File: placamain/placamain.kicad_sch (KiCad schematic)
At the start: 38 parts, among them J1 Conn_01x10_Pin, J2 Conn_01x10_Pin, Q1 PN3643, U10 LF356, U2 LF356, U3 LF356, U4 LF356, U5 AD548JN, U6 LF356, U7 LF356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

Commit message: empieza parte de los comparadores LM393
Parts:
- added C5: valor?, symbol Device:C_Small
- added D2: ?, symbol Device:D_Zener
- added Q2: BC559, symbol Simulation_SPICE:PNP
- added R7: 7,5K, symbol Device:R
- D1: value D_Zener -> ?
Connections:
- net -15V: now also C5.2, Q2.3 (E), R7.1
- net at J1.10 (Pin_10), R9.1: now also Q2.1 (C)
- net at D1.1 (K), J1.6 (Pin_6), U2.3 (+): now also D2.1 (K)
- new net: C5.1, D2.2 (A), Q2.2 (B), R7.2
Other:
- moved on the sheet: U9A, U9B, U9C

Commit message: Resistencias lado comparador
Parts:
- added R1: 3,9k, symbol Device:R
- added R2: 4,8k, symbol Device:R
- added R3: 3,6k, symbol Device:R
- added w4: 0, symbol Device:R
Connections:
- net GND: now also R2.2
- net at U9.6 (-): now also R2.1, R3.1
- net at U9.7: now also R1.2
- net at J1.4 (Pin_4): now also w4.2
- net at U9.4 (V-): now also R3.2
- new net: R1.1, w4.1
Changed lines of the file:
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@@
   (junction (at 53.34 185.42) (diameter 0) (color 0 0 0 0)
   )
+  (junction (at 38.1 24.13) (diameter 0) (color 0 0 0 0)
+  )
   (junction (at 50.8 147.32) (diameter 0) (color 0 0 0 0)
   )
@@
     (stroke (width 0) (type default))
   )
+  (wire (pts (xy 52.07 21.59) (xy 52.07 29.21))
+    (stroke (width 0) (type default))
+  )
   (wire (pts (xy 57.15 137.16) (xy 48.26 137.16))
     (stroke (width 0) (type default))
@@
     (stroke (width 0) (type default))
   )
+  (wire (pts (xy 20.32 142.24) (xy 45.72 142.24))
+    (stroke (width 0) (type default))
+  )
   (wire (pts (xy 119.38 107.95) (xy 119.38 115.57))
     (stroke (width 0) (type default))
@@
     (stroke (width 0) (type default))
   )
+  (wire (pts (xy 45.72 21.59) (xy 52.07 21.59))
+    (stroke (width 0) (type default))
+  )
+  (wire (pts (xy 54.61 26.67) (xy 54.61 58.42))
+    (stroke (width 0) (type default))
+  )
   (wire (pts (xy 69.85 106.68) (xy 77.47 106.68))
     (stroke (width 0) (type default))
@@
     (stroke (width 0) (type default))
   )
+  (wire (pts (xy 38.1 21.59) (xy 38.1 24.13))
+    (stroke (width 0) (type default))
+  )
   (wire (pts (xy 67.31 180.34) (xy 71.12 180.34))
     (stroke (width 0) (type default))
@@
     (stroke (width 0) (type default))
   )
+  (wire (pts (xy 45.72 142.24) (xy 45.72 147.32))
+    (stroke (width 0) (type default))
+  )
+  (wire (pts (xy 27.94 54.61) (xy 33.02 54.61))
+    (stroke (width 0) (type default))
+  )
   (wire (pts (xy 69.85 163.83) (xy 69.85 168.91))
     (stroke (width 0) (type default))
@@
     (stroke (width 0) (type default))
   )
+  (wire (pts (xy 40.64 58.42) (xy 54.61 58.42))
+    (stroke (width 0) (type default))
+  )
   (wire (pts (xy 77.47 173.99) (xy 77.47 185.42))
     (stroke (width 0) (type default))
   )
+  (wire (pts (xy 20.32 54.61) (xy 20.32 142.24))
+    (stroke (width 0) (type default))
+  )
   (wire (pts (xy 38.1 165.1) (xy 50.8 165.1))
     (stroke (width 0) (type default))
@@
     (stroke (width 0) (type default))
   )
+  (wire (pts (xy 55.88 52.07) (xy 48.26 52.07))
+    (stroke (width 0) (type default))
+  )
   (wire (pts (xy 26.67 161.29) (xy 55.88 161.29))
     (stroke (width 0) (type default))
@@
     (stroke (width 0) (type default))
   )
+  (wire (pts (xy 38.1 24.13) (xy 27.94 24.13))
+    (stroke (width 0) (type default))
+  )
   (wire (pts (xy 106.68 147.32) (xy 106.68 146.05))
     (stroke (width 0) (type default))
@@
     (stroke (width 0) (type default))
   )
+  (wire (pts (xy 45.72 26.67) (xy 54.61 26.67))
+    (stroke (width 0) (type default))
+  )
   (wire (pts (xy 53.34 180.34) (xy 53.34 185.42))
     (stroke (width 0) (type default))
@@
     (stroke (width 0) (type default))
   )
+  (wire (pts (xy 20.32 46.99) (xy 20.32 16.51))
+    (stroke (width 0) (type default))
+  )
   (wire (pts (xy 53.34 88.9) (xy 57.15 88.9))
     (stroke (width 0) (type default))
@@
     (stroke (width 0) (type default))
   )
+  (wire (pts (xy 20.32 16.51) (xy 38.1 16.51))
+    (stroke (width 0) (type default))
+  )
   (wire (pts (xy 121.92 143.51) (xy 121.92 147.32))
     (stroke (width 0) (type default))
@@
     (stroke (width 0) (type default))
   )
+  (wire (pts (xy 55.88 16.51) (xy 55.88 52.07))
+    (stroke (width 0) (type default))
+  )
+  (wire (pts (xy 45.72 16.51) (xy 55.88 16.51))
+    (stroke (width 0) (type default))
+  )
   (wire (pts (xy 86.36 123.19) (xy 86.36 114.3))
     (stroke (width 0) (type default))
@@
   )
   (wire (pts (xy 146.05 110.49) (xy 147.32 110.49))
+    (stroke (width 0) (type default))
+  )
+  (wire (pts (xy 38.1 24.13) (xy 38.1 26.67))
+    (stroke (width 0) (type default))
+  )
+  (wire (pts (xy 27.94 24.13) (xy 27.94 54.61))
     (stroke (width 0) (type default))
   )
@@
     )
   )
+  (symbol (lib_id "Device:R") (at 20.32 50.8 0) (unit 1)
+    (in_bom yes) (on_board yes) (dnp no) (fields_autoplaced)
+    (property "Reference" "w4" (at 22.86 50.165 0)
+      (effects (font (size 1.27 1.27)) (justify left))
+    )
+    (property "Value" "0" (at 22.86 52.705 0)
+      (effects (font (size 1.27 1.27)) (justify left))
+    )
+    (property "Footprint" "" (at 18.542 50.8 90)
+      (effects (font (size 1.27 1.27)) hide)
+    )
+    (property "Datasheet" "~" (at 20.32 50.8 0)
+      (effects (font (size 1.27 1.27)) hide)
+    )
+    (pin "1")
+    (pin "2")
+    (instances
+      (project "placamain"
+        (path "/97204b45-cd64-488c-9a18-9c4a16d0810d"
+          (reference "w4") (unit 1)
+        )
+      )
+    )
+  )
   (symbol (lib_id "Amplifier_Operational:LF356") (at 170.18 101.6 0) (unit 1)
     (in_bom yes) (on_board yes) (dnp no)
@@
     )
   )
+  (symbol (lib_id "Device:R") (at 41.91 16.51 90) (unit 1)
+    (in_bom yes) (on_board yes) (dnp no)
+    (property "Reference" "R1" (at 44.45 13.97 90)
+      (effects (font (size 1.27 1.27)) (justify right))
+    )
+    (property "Value" "3,9k" (at 39.37 13.97 90)
+      (effects (font (size 1.27 1.27)) (justify right))
+    )
+    (property "Footprint" "" (at 41.91 18.288 90)
+      (effects (font (size 1.27 1.27)) hide)
+    )
+    (property "Datasheet" "~" (at 41.91 16.51 0)
+      (effects (font (size 1.27 1.27)) hide)
+    )
+    (pin "1")
+    (pin "2")
+    (instances
+      (project "placamain"
+        (path "/97204b45-cd64-488c-9a18-9c4a16d0810d"
+          (reference "R1") (unit 1)
+        )
+      )
+    )
+  )
+  (symbol (lib_id "Device:R") (at 41.91 26.67 90) (unit 1)
+    (in_bom yes) (on_board yes) (dnp no)
+    (property "Reference" "R3" (at 44.45 24.13 90)
+      (effects (font (size 1.27 1.27)) (justify right))
+    )
+    (property "Value" "3,6k" (at 39.37 24.13 90)
+      (effects (font (size 1.27 1.27)) (justify right))
+    )
+    (property "Footprint" "" (at 41.91 28.448 90)
+      (effects (font (size 1.27 1.27)) hide)
+    )
+    (property "Datasheet" "~" (at 41.91 26.67 0)
+      (effects (font (size 1.27 1.27)) hide)
+    )
+    (pin "1")
+    (pin "2")
+    (instances
+      (project "placamain"
+        (path "/97204b45-cd64-488c-9a18-9c4a16d0810d"
+          (reference "R3") (unit 1)
+        )
+      )
+    )
+  )
   (symbol (lib_id "Device:D_Zener") (at 66.04 163.83 0) (unit 1)
     (in_bom yes) (on_board yes) (dnp no)
@@
         (path "/97204b45-cd64-488c-9a18-9c4a16d0810d"
           (reference "C3") (unit 1)
+        )
+      )
+    )
+  )
+  (symbol (lib_id "Device:R") (at 41.91 21.59 90) (unit 1)
+    (in_bom yes) (on_board yes) (dnp no)
+    (property "Reference" "R2" (at 44.45 19.05 90)
+      (effects (font (size 1.27 1.27)) (justify right))
+    )
+    (property "Value" "4,8k" (at 39.37 19.05 90)
+      (effects (font (size 1.27 1.27)) (justify right))
+    )
+    (property "Footprint" "" (at 41.91 23.368 90)
+      (effects (font (size 1.27 1.27)) hide)
+    )
+    (property "Datasheet" "~" (at 41.91 21.59 0)
+      (effects (font (size 1.27 1.27)) hide)
+    )
+    (pin "1")
+    (pin "2")
+    (instances
+      (project "placamain"
+        (path "/97204b45-cd64-488c-9a18-9c4a16d0810d"
+          (reference "R2") (unit 1)
         )
       )
@@
         )
       )
+    )
+  )
+  (symbol (lib_id "power:GND") (at 52.07 29.21 0) (unit 1)
+    (in_bom yes) (on_board yes) (dnp no) (fields_autoplaced)
+    (property "Reference" "#PWR012" (at 52.07 35.56 0)
+      (effects (font (size 1.27 1.27)) hide)
+    )
+    (property "Value" "GND" (at 52.07 34.29 0)
+      (effects (font (size 1.27 1.27)))
+    )
+    (property "Footprint" "" (at 52.07 29.21 0)
+      (effects (font (size 1.27 1.27)) hide)
+    )
+    (property "Datasheet" "" (at 52.07 29.21 0)
+      (effects (font (size 1.27 1.27)) hide)
+    )
+    (pin "1")
+    (instances
+      (project "placamain"
+        (path "/97204b45-cd64-488c-9a18-9c4a16d0810d"
+          (reference "#PWR012") (unit 1)
+        )
+      )

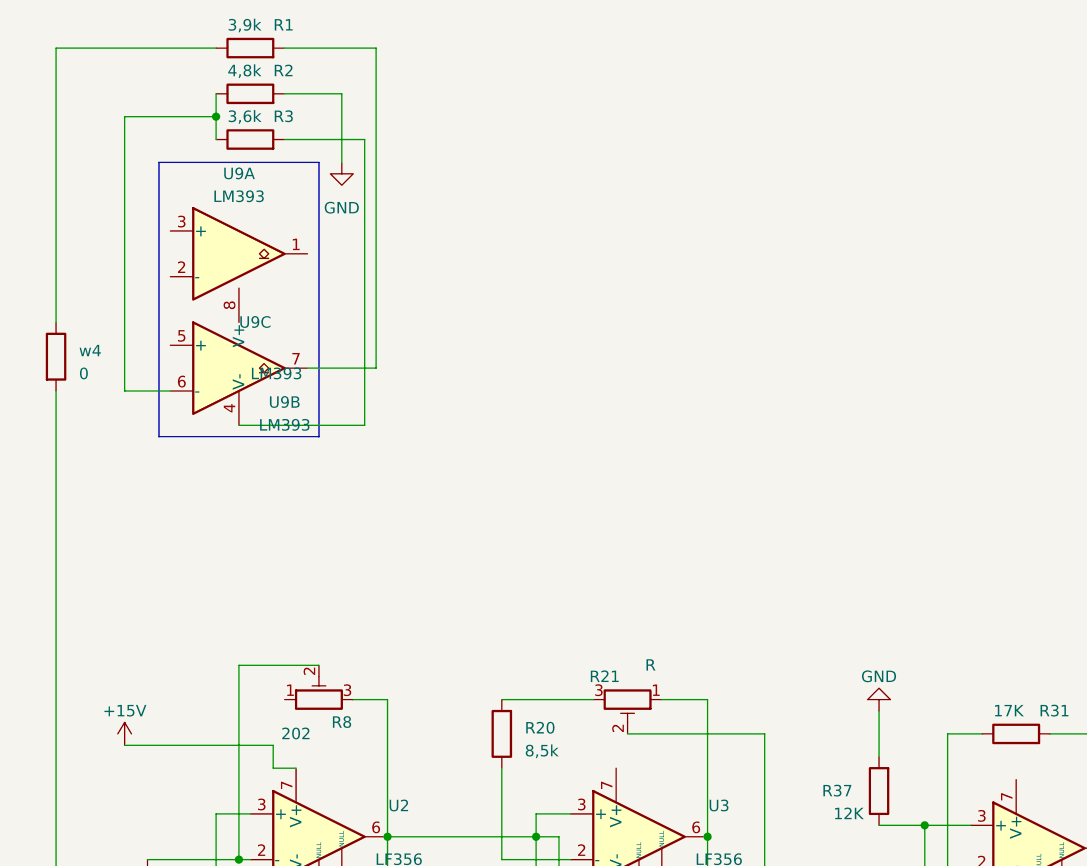
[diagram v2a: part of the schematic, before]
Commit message: Agrego comparador U8
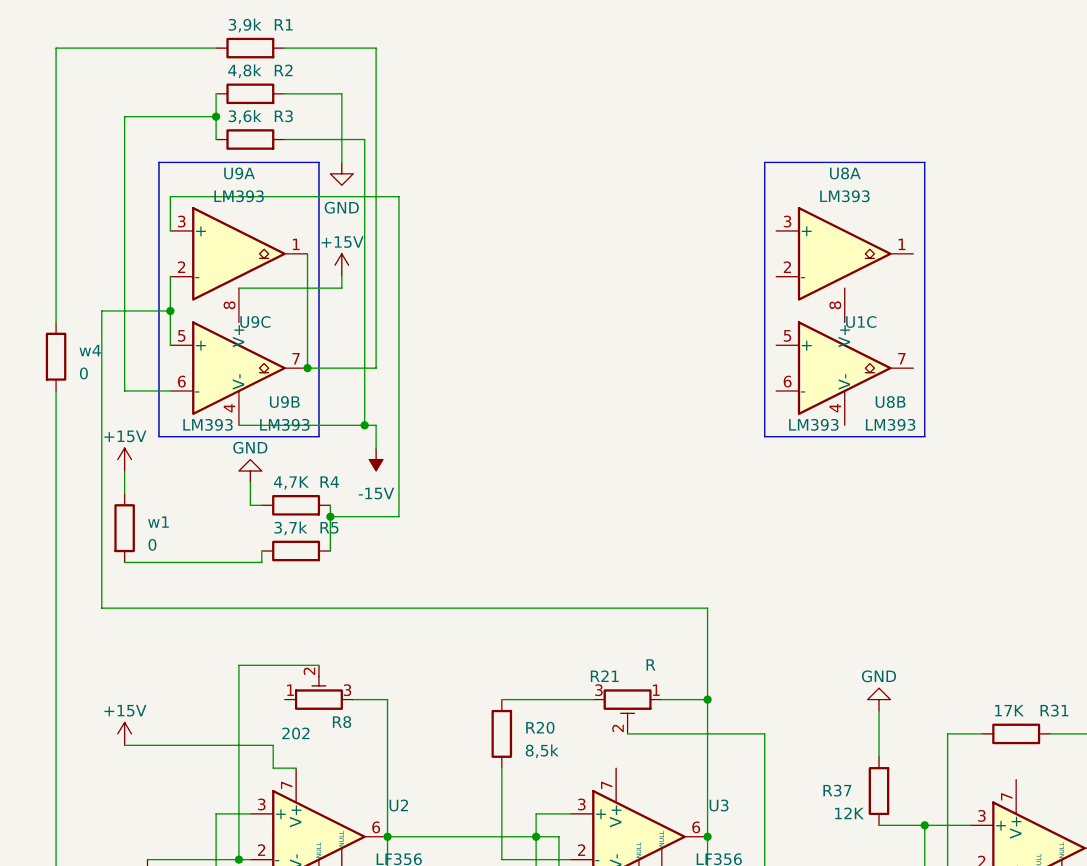
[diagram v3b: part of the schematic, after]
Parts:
- added R4: 4,7K, symbol Device:R
- added R5: 3,7k, symbol Device:R
- added U1, U8: LM393, symbol Comparator:LM393
- added w1: 0, symbol Device:R
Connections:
- net +15V: now also U9.8 (V+), w1.1
- net -15V: now also R3.2, U9.4 (V-)
- net GND: now also R4.1
- net at J1.3 (Pin_3), R21.1, U3.6: now also U9.2 (-), U9.5 (+)
- net at R1.2, U9.7: now also U9.1
- net at U9.3 (+): now also R4.2, R5.2
- new net: R5.1, w1.2

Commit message: Agrego CI12
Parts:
- added R22, R24: 3,7k, symbol Device:R
- added R23: 4,8k, symbol Device:R
- added R25: 4,8K, symbol Device:R
- added R26: 3,9k, symbol Device:R
- added R27: R, symbol Device:R_Potentiometer_Trim
- added RN1: R_Pack05_SIP, Resistor_THT:R_Array_SIP10, symbol Device:R_Pack05_SIP
- added U12: LF356, symbol Amplifier_Operational:LF356
- added w2, w23, w6: 0, symbol Device:R
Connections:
- net +15V: now also R27.2, U12.7 (V+), w2.1
- net -15V: now also R24.2, U12.4 (V-)
- net GND: now also R23.2, R25.2, w23.2
- net at U8.5 (+): now also U8.2 (-), w6.1
- net at U8.6 (-): now also R24.1, R25.1
- net at U8.7: now also U8.1
- net at U8.3 (+): now also R22.1, R23.1
- net at U1.8 (V+): now also R22.2, w2.2
- new net: RN1.8 (R4.2), w23.1
- new net: RN1.5 (R3.1), w6.2
- new net: R27.1, U12.1 (NULL)
- new net: R27.3, U12.5 (NULL)
- new net: RN1.1 (R1.1), U12.6
- new net: RN1.2 (R1.2), RN1.3 (R2.1), U12.2 (-)
- new net: RN1.6 (R3.2), RN1.7 (R4.1), U12.3 (+)
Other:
- moved on the sheet: U1C, U8A, U8B

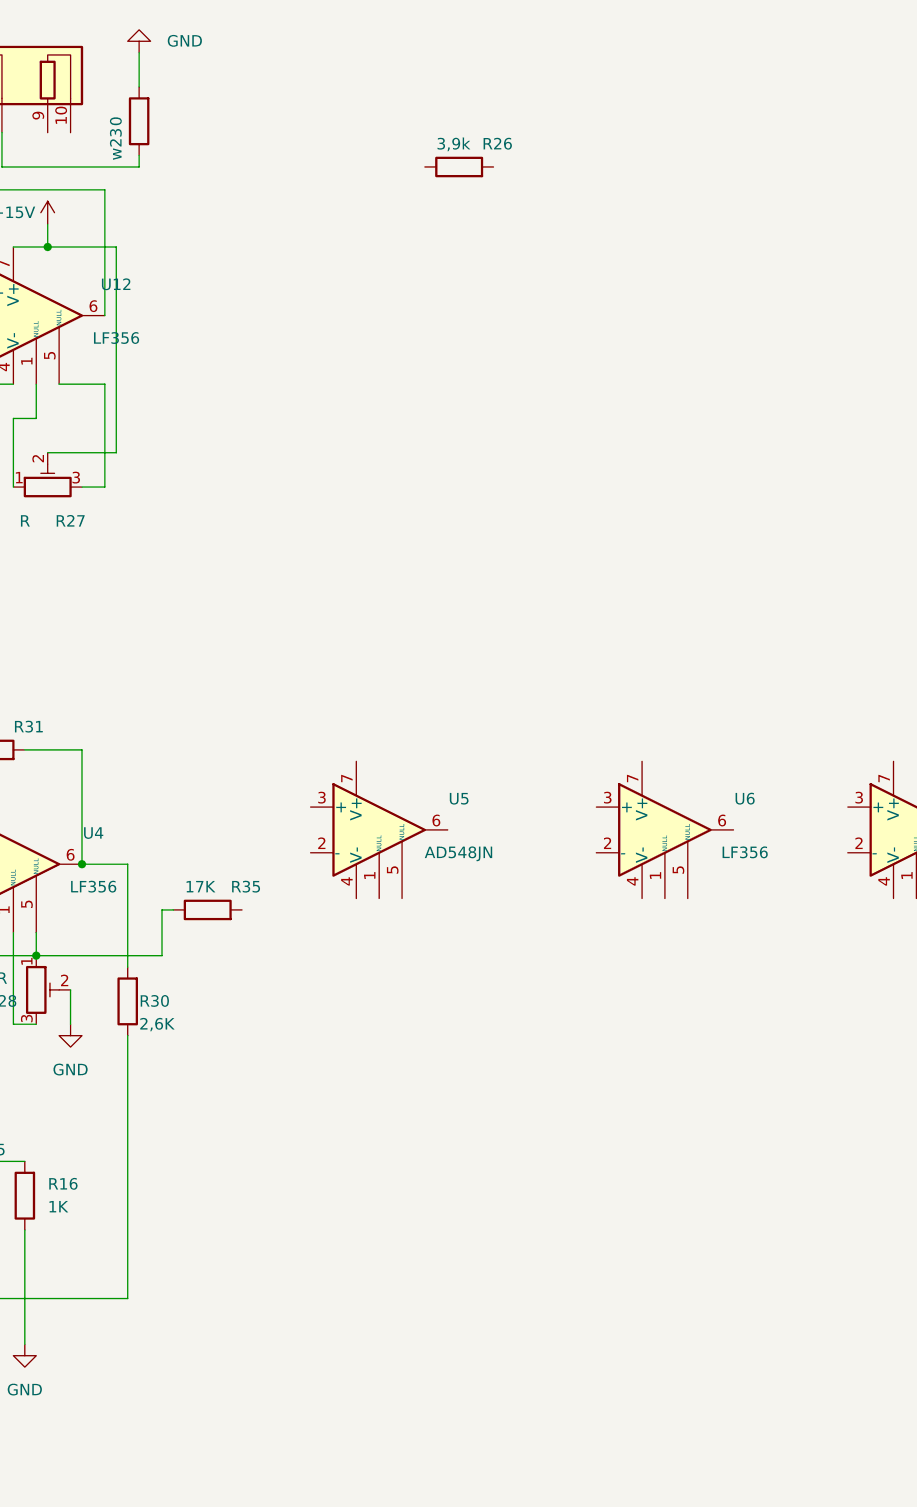
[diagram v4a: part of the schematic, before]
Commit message: agrego DG211 , no encrontre la libreria de este, puse otro componente pero este componente su pin12 dice No conect , el del DG es de +5 volts
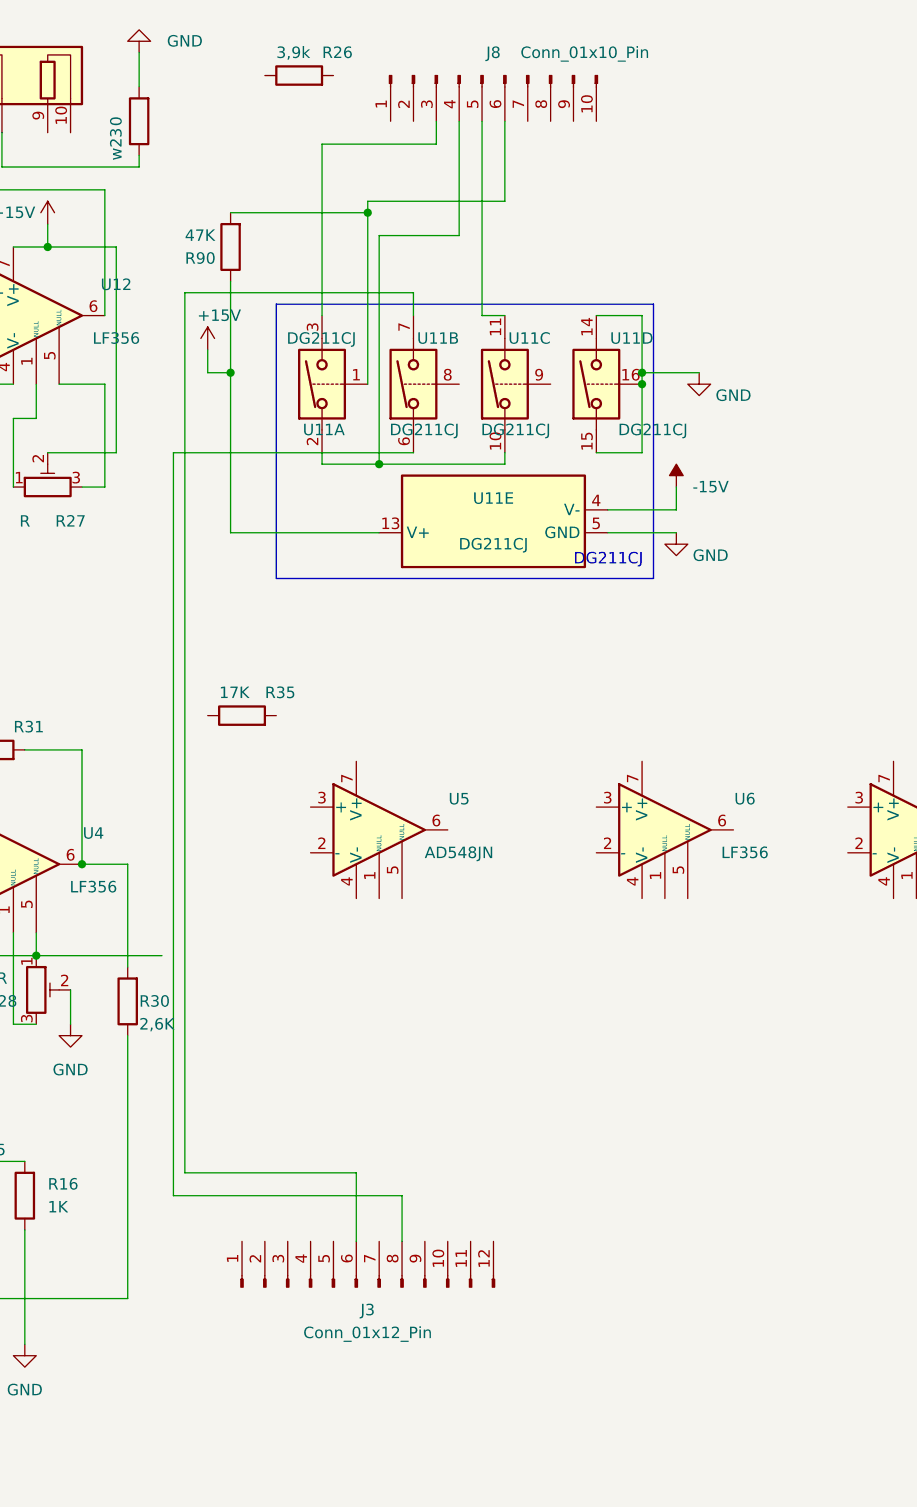
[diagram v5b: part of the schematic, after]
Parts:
- added J3: Conn_01x12_Pin, symbol Connector:Conn_01x12_Pin
- added J8: Conn_01x10_Pin, symbol Connector:Conn_01x10_Pin
- added R90: 47K, symbol Device:R
- added U11: DG211CJ, Package_DIP:DIP-16_W7.62mm, symbol Analog_Switch:DG308AxJ
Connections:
- net +15V: now also R90.1, U11.13 (V+)
- net -15V: now also U11.4 (V-)
- net GND: now also U11.14, U11.15, U11.16, U11.5 (GND)
- net at R28.1, R31.1, U4.2 (-)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: no longer R35.1
- new net: J8.6 (Pin_6), R90.2, U11.1
- new net: J8.4 (Pin_4), U11.10, U11.2
- new net: J8.3 (Pin_3), U11.3
- new net: J3.6 (Pin_6), U11.7
- new net: J3.8 (Pin_8), U11.6
- new net: J8.5 (Pin_5), U11.11
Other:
- note added: "DG211CJ"
- moved on the sheet: R26, R35

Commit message: pureba de equipo funcionando
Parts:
- added C21: C, symbol Device:C
- added J4: Conn_01x10_Pin, symbol Connector:Conn_01x10_Pin
- added Q3: PN3643, symbol Simulation_SPICE:NPN
- added R29: R, symbol Device:R_Potentiometer_Trim
- added R36: 25k, symbol Device:R
- added R38, R58: RV, symbol Device:R_Potentiometer_Trim
- added R39: 2,2k, symbol Device:R
- added R40: 5k, symbol Device:R
- added R42: 3,7k, symbol Device:R
- added R43, R46: 32k, symbol Device:R
- added R45: 34k, symbol Device:R
- added R47: 12M, symbol Device:R
- added R48: 50k, symbol Device:R
- added R49: 4k, symbol Device:R
- added R50, R62: 1k, symbol Device:R
- added R53, R54: 1,8k, symbol Device:R
- added R55: 90k, symbol Device:R
- added R59: 100k, symbol Device:R
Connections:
- net +15V: now also R42.1
- net GND: now also J3.10 (Pin_10), Q3.3 (E), R38.2, R39.1, R53.1, R54.1, R59.1
- net at R28.1, R31.1, U4.2 (-)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: now also R35.1
- net at R26.1: now also U8.1, U8.7
- net at R26.2: now also J3.12 (Pin_12)
- net at J3.11 (Pin_11): now also R36.1
- net at J3.2 (Pin_2): now also R42.2
- net at J3.3 (Pin_3): now also R54.2
- net at J3.4 (Pin_4): now also R53.2
- net at J3.5 (Pin_5): now also R40.1
- net at J3.7 (Pin_7): now also R49.1
- net at J3.8 (Pin_8), U11.6: now also R48.2
- net at J3.9 (Pin_9): now also R47.1
- net at U11.8: now also Q3.1 (C)
- net at U5.2 (-): now also R43.1, R45.2, R46.2, R47.2, R48.1
- net at U5.3 (+): now also R29.1, R50.2
- net at U5.6: now also R35.2, R43.2
- net at U7.3 (+): now also R62.2
- net at U11.9: now also J8.2 (Pin_2)
- net at U6.1 (NULL): now also R38.3
- net at U6.3 (+): now also R58.1
- net at U6.5 (NULL): now also R38.1
- net at U6.6: now also R62.1
- new net: R29.2, R45.1
- new net: R29.3, R36.2
- new net: R58.2, R59.2
- new net: R55.2, R58.3
- new net: R46.1, R49.2, R50.1
- new net: J4.9 (Pin_9), R55.1
- new net: Q3.2 (B), R39.2, R40.2
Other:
- moved on the sheet: R26, R35, U10, U6, U7
